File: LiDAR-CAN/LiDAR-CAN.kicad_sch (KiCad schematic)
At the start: 32 parts, among them J1 XT30(2+2), J2 XT30(2+2), J3 G7LX-A88S7-BP-G/Y, J4 XT30(2+2)

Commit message: Add CAN and MCU placement
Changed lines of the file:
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@@
 	)
 	(junction
-		(at 270.51 127)
+		(at 158.75 165.1)
 		(diameter 0)
 		(color 0 0 0 0)
 	)
 	(junction
-		(at 158.75 120.65)
+		(at 270.51 127)
 		(diameter 0)
 		(color 0 0 0 0)
 	)
 	(junction
-		(at 158.75 167.64)
+		(at 158.75 123.19)
 		(diameter 0)
 		(color 0 0 0 0)
 	)
 	(junction
-		(at 158.75 162.56)
+		(at 260.35 222.25)
 		(diameter 0)
 		(color 0 0 0 0)
 	)
 	(junction
-		(at 260.35 222.25)
+		(at 158.75 160.02)
 		(diameter 0)
 		(color 0 0 0 0)
 	)
 	(junction
-		(at 158.75 123.19)
+		(at 158.75 120.65)
 		(diameter 0)
 		(color 0 0 0 0)
@@
 	)
 	(junction
-		(at 158.75 160.02)
+		(at 158.75 162.56)
 		(diameter 0)
 		(color 0 0 0 0)
 	)
 	(junction
-		(at 266.7 209.55)
+		(at 158.75 128.27)
 		(diameter 0)
 		(color 0 0 0 0)
 	)
 	(junction
-		(at 158.75 128.27)
+		(at 266.7 209.55)
 		(diameter 0)
 		(color 0 0 0 0)
@@
 	)
 	(junction
-		(at 158.75 165.1)
+		(at 304.8 209.55)
 		(diameter 0)
 		(color 0 0 0 0)
 	)
 	(junction
-		(at 304.8 209.55)
+		(at 292.1 209.55)
 		(diameter 0)
 		(color 0 0 0 0)
 	)
 	(junction
-		(at 292.1 209.55)
+		(at 158.75 167.64)
 		(diameter 0)
 		(color 0 0 0 0)
@@
 	(wire
 		(pts
-			(xy 152.4 123.19) (xy 158.75 123.19)
-		)
-		(stroke
-			(width 0)
-			(type default)
-		)
-	)
-	(wire
-		(pts
 			(xy 152.4 54.61) (xy 152.4 57.15)
 		)
@@
 	(wire
 		(pts
-			(xy 152.4 128.27) (xy 158.75 128.27)
-		)
-		(stroke
-			(width 0)
-			(type default)
-		)
-	)
-	(wire
-		(pts
 			(xy 158.75 123.19) (xy 181.61 123.19)
 		)
@@
 	(wire
 		(pts
-			(xy 152.4 162.56) (xy 158.75 162.56)
+			(xy 152.4 120.65) (xy 158.75 120.65)
 		)
 		(stroke
@@
 	(wire
 		(pts
-			(xy 152.4 165.1) (xy 158.75 165.1)
+			(xy 189.23 208.28) (xy 189.23 165.1)
 		)
 		(stroke
@@
 	(wire
 		(pts
-			(xy 189.23 208.28) (xy 189.23 165.1)
+			(xy 152.4 125.73) (xy 158.75 125.73)
 		)
 		(stroke
@@
 	(wire
 		(pts
+			(xy 152.4 167.64) (xy 158.75 167.64)
+		)
+		(stroke
+			(width 0)
+			(type default)
+		)
+	)
+	(wire
+		(pts
 			(xy 210.82 76.2) (xy 210.82 81.28)
 		)
@@
 	(wire
 		(pts
-			(xy 304.8 209.55) (xy 304.8 212.09)
+			(xy 152.4 160.02) (xy 158.75 160.02)
 		)
 		(stroke
@@
 	(wire
 		(pts
-			(xy 266.7 209.55) (xy 266.7 212.09)
+			(xy 304.8 209.55) (xy 304.8 212.09)
 		)
 		(stroke
@@
 	(wire
 		(pts
-			(xy 158.75 160.02) (xy 152.4 160.02)
+			(xy 266.7 209.55) (xy 266.7 212.09)
 		)
 		(stroke
@@
 	(wire
 		(pts
-			(xy 152.4 167.64) (xy 158.75 167.64)
-		)
-		(stroke
-			(width 0)
-			(type default)
-		)
-	)
-	(wire
-		(pts
 			(xy 332.74 203.2) (xy 330.2 205.74)
 		)
@@
 	(wire
 		(pts
+			(xy 152.4 165.1) (xy 158.75 165.1)
+		)
+		(stroke
+			(width 0)
+			(type default)
+		)
+	)
+	(wire
+		(pts
 			(xy 260.35 222.25) (xy 266.7 222.25)
 		)
@@
 	(wire
 		(pts
-			(xy 270.51 127) (xy 279.4 127)
+			(xy 152.4 162.56) (xy 158.75 162.56)
 		)
 		(stroke
@@
 	(wire
 		(pts
-			(xy 158.75 120.65) (xy 179.07 120.65)
+			(xy 270.51 127) (xy 279.4 127)
 		)
 		(stroke
@@
 	(wire
 		(pts
-			(xy 241.3 93.98) (xy 285.75 93.98)
+			(xy 158.75 120.65) (xy 179.07 120.65)
 		)
 		(stroke
@@
 	(wire
 		(pts
-			(xy 266.7 127) (xy 266.7 129.54)
+			(xy 241.3 93.98) (xy 285.75 93.98)
 		)
 		(stroke
@@
 	(wire
 		(pts
-			(xy 179.07 120.65) (xy 179.07 88.9)
+			(xy 266.7 127) (xy 266.7 129.54)
 		)
 		(stroke
@@
 	(wire
 		(pts
-			(xy 317.5 205.74) (xy 330.2 205.74)
+			(xy 152.4 128.27) (xy 158.75 128.27)
 		)
 		(stroke
@@
 	(wire
 		(pts
-			(xy 241.3 104.14) (xy 285.75 104.14)
+			(xy 179.07 120.65) (xy 179.07 88.9)
 		)
 		(stroke
@@
 	(wire
 		(pts
-			(xy 254 212.09) (xy 254 203.2)
+			(xy 317.5 205.74) (xy 330.2 205.74)
 		)
 		(stroke
@@
 	(wire
 		(pts
-			(xy 262.89 111.76) (xy 262.89 118.11)
+			(xy 241.3 104.14) (xy 285.75 104.14)
 		)
 		(stroke
@@
 	(wire
 		(pts
-			(xy 215.9 203.2) (xy 194.31 203.2)
+			(xy 254 212.09) (xy 254 203.2)
 		)
 		(stroke
@@
 	(wire
 		(pts
-			(xy 152.4 125.73) (xy 158.75 125.73)
+			(xy 262.89 111.76) (xy 262.89 118.11)
 		)
 		(stroke
@@
 	(wire
 		(pts
-			(xy 285.75 116.84) (xy 279.4 116.84)
+			(xy 215.9 203.2) (xy 194.31 203.2)
 		)
 		(stroke
@@
 	(wire
 		(pts
-			(xy 215.9 226.06) (xy 171.45 226.06)
+			(xy 285.75 116.84) (xy 279.4 116.84)
 		)
 		(stroke
@@
 	(wire
 		(pts
-			(xy 152.4 120.65) (xy 158.75 120.65)
+			(xy 215.9 226.06) (xy 171.45 226.06)
 		)
 		(stroke
@@
 		)
 	)
+	(wire
+		(pts
+			(xy 152.4 123.19) (xy 158.75 123.19)
+		)
+		(stroke
+			(width 0)
+			(type default)
+		)
+	)
 	(symbol
 		(lib_id "Connector:TestPoint_Small")
@@
 		)
 		(pin "SPI1_MISO" input
-			(at 152.4 125.73 0)
+			(at 152.4 165.1 0)
 			(effects
 				(font
@@
 		)
 		(pin "SPI1_MOSI" output
-			(at 152.4 123.19 0)
+			(at 152.4 162.56 0)
 			(effects
 				(font
@@
 		)
 		(pin "SPI1_NSS" output
-			(at 152.4 128.27 0)
+			(at 152.4 167.64 0)
 			(effects
 				(font
@@
 		)
 		(pin "SPI1_SCK" output
-			(at 152.4 120.65 0)
+			(at 152.4 160.02 0)
 			(effects
 				(font
@@
 		)
 		(pin "SPI2_MISO" input
-			(at 152.4 162.56 0)
+			(at 152.4 125.73 0)
 			(effects
 				(font
@@
 		)
 		(pin "SPI2_MOSI" output
-			(at 152.4 165.1 0)
+			(at 152.4 123.19 0)
 			(effects
 				(font
@@
 		)
 		(pin "SPI2_NSS" output
-			(at 152.4 167.64 0)
+			(at 152.4 128.27 0)
 			(effects
 				(font
@@
 		)
 		(pin "SPI2_SCK" output
-			(at 152.4 160.02 0)
+			(at 152.4 120.65 0)
 			(effects
 				(font

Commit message: Update complete first placement
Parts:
- added H3: MountingHole, MountingHole:MountingHole_2.2mm_M2, symbol Mechanical:MountingHole
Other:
- moved on the sheet: FID1, FID2, H1, H2
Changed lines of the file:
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@@
 	(text_box "Mechanicals"
 		(exclude_from_sim no)
-		(at 50.8 215.9 0)
-		(size 88.9 25.4)
+		(at 38.1 215.9 0)
+		(size 101.6 25.4)
 		(margins 0.9525 0.9525 0.9525 0.9525)
 		(stroke
@@
 	)
 	(symbol
+		(lib_id "Mechanical:MountingHole")
+		(at 120.65 228.6 0)
+		(unit 1)
+		(exclude_from_sim yes)
+		(in_bom no)
+		(on_board yes)
+		(dnp no)
+		(fields_autoplaced yes)
+		(property "Reference" "H3"
+			(at 123.19 227.3299 0)
+			(effects
+				(font
+					(size 1.27 1.27)
+				)
+				(justify left)
+			)
+		)
+		(property "Value" "MountingHole"
+			(at 123.19 229.8699 0)
+			(effects
+				(font
+					(size 1.27 1.27)
+				)
+				(justify left)
+			)
+		)
+		(property "Footprint" "MountingHole:MountingHole_2.2mm_M2"
+			(at 120.65 228.6 0)
+			(effects
+				(font
+					(size 1.27 1.27)
+				)
+				(hide yes)
+			)
+		)
+		(property "Datasheet" "~"
+			(at 120.65 228.6 0)
+			(effects
+				(font
+					(size 1.27 1.27)
+				)
+				(hide yes)
+			)
+		)
+		(property "Description" "Mounting Hole without connection"
+			(at 120.65 228.6 0)
+			(effects
+				(font
+					(size 1.27 1.27)
+				)
+				(hide yes)
+			)
+		)
+		(instances
+			(project "LiDAR-CAN"
+				(path "/56db6f21-0e4a-4321-bd8a-db37f1842dd9"
+					(reference "H3")
+					(unit 1)
+				)
+			)
+		)
+	)
+	(symbol
 		(lib_id "Device:R_US")
 		(at 254 121.92 0)
@@
 	(symbol
 		(lib_id "Mechanical:Fiducial")
-		(at 63.5 228.6 0)
+		(at 50.8 228.6 0)
 		(unit 1)
 		(exclude_from_sim yes)
@@
 		(fields_autoplaced yes)
 		(property "Reference" "FID1"
-			(at 66.04 227.3299 0)
+			(at 53.34 227.3299 0)
 			(effects
 				(font
@@
 		)
 		(property "Value" "Fiducial"
-			(at 66.04 229.8699 0)
+			(at 53.34 229.8699 0)
 			(effects
 				(font
@@
 		)
 		(property "Footprint" "Fiducial:Fiducial_1.5mm_Mask3mm"
-			(at 63.5 228.6 0)
+			(at 50.8 228.6 0)
 			(effects
 				(font
@@
 		)
 		(property "Datasheet" "~"
-			(at 63.5 228.6 0)
+			(at 50.8 228.6 0)
 			(effects
 				(font
@@
 		)
 		(property "Description" "Fiducial Marker"
-			(at 63.5 228.6 0)
+			(at 50.8 228.6 0)
 			(effects
 				(font
@@
 	(symbol
 		(lib_id "Mechanical:Fiducial")
-		(at 76.2 228.6 0)
+		(at 63.5 228.6 0)
 		(unit 1)
 		(exclude_from_sim yes)
@@
 		(fields_autoplaced yes)
 		(property "Reference" "FID2"
-			(at 78.74 227.3299 0)
+			(at 66.04 227.3299 0)
 			(effects
 				(font
@@
 		)
 		(property "Value" "Fiducial"
-			(at 78.74 229.8699 0)
+			(at 66.04 229.8699 0)
 			(effects
 				(font
@@
 		)
 		(property "Footprint" "Fiducial:Fiducial_1.5mm_Mask3mm"
-			(at 76.2 228.6 0)
+			(at 63.5 228.6 0)
 			(effects
 				(font
@@
 		)
 		(property "Datasheet" "~"
-			(at 76.2 228.6 0)
+			(at 63.5 228.6 0)
 			(effects
 				(font
@@
 		)
 		(property "Description" "Fiducial Marker"
-			(at 76.2 228.6 0)
+			(at 63.5 228.6 0)
 			(effects
 				(font
@@
 	(symbol
 		(lib_id "Mechanical:MountingHole")
-		(at 95.25 228.6 0)
+		(at 82.55 228.6 0)
 		(unit 1)
 		(exclude_from_sim yes)
@@
 		(fields_autoplaced yes)
 		(property "Reference" "H1"
-			(at 97.79 227.3299 0)
+			(at 85.09 227.3299 0)
 			(effects
 				(font
@@
 		)
 		(property "Value" "MountingHole"
-			(at 97.79 229.8699 0)
+			(at 85.09 229.8699 0)
 			(effects
 				(font
@@
 		)
 		(property "Footprint" "MountingHole:MountingHole_2.2mm_M2"
-			(at 95.25 228.6 0)
+			(at 82.55 228.6 0)
 			(effects
 				(font
@@
 		)
 		(property "Datasheet" "~"
-			(at 95.25 228.6 0)
+			(at 82.55 228.6 0)
 			(effects
 				(font
@@
 		)
 		(property "Description" "Mounting Hole without connection"
-			(at 95.25 228.6 0)
+			(at 82.55 228.6 0)
 			(effects
 				(font
@@
 	(symbol
 		(lib_id "Mechanical:MountingHole")
-		(at 114.3 228.6 0)
+		(at 101.6 228.6 0)
 		(unit 1)
 		(exclude_from_sim yes)
@@
 		(fields_autoplaced yes)
 		(property "Reference" "H2"
-			(at 116.84 227.3299 0)
+			(at 104.14 227.3299 0)
 			(effects
 				(font
@@
 		)
 		(property "Value" "MountingHole"
-			(at 116.84 229.8699 0)
+			(at 104.14 229.8699 0)
 			(effects
 				(font
@@
 		)
 		(property "Footprint" "MountingHole:MountingHole_2.2mm_M2"
-			(at 114.3 228.6 0)
+			(at 101.6 228.6 0)
 			(effects
 				(font
@@
 		)
 		(property "Datasheet" "~"
-			(at 114.3 228.6 0)
+			(at 101.6 228.6 0)
 			(effects
 				(font
@@
 		)
 		(property "Description" "Mounting Hole without connection"
-			(at 114.3 228.6 0)
+			(at 101.6 228.6 0)
 			(effects
 				(font

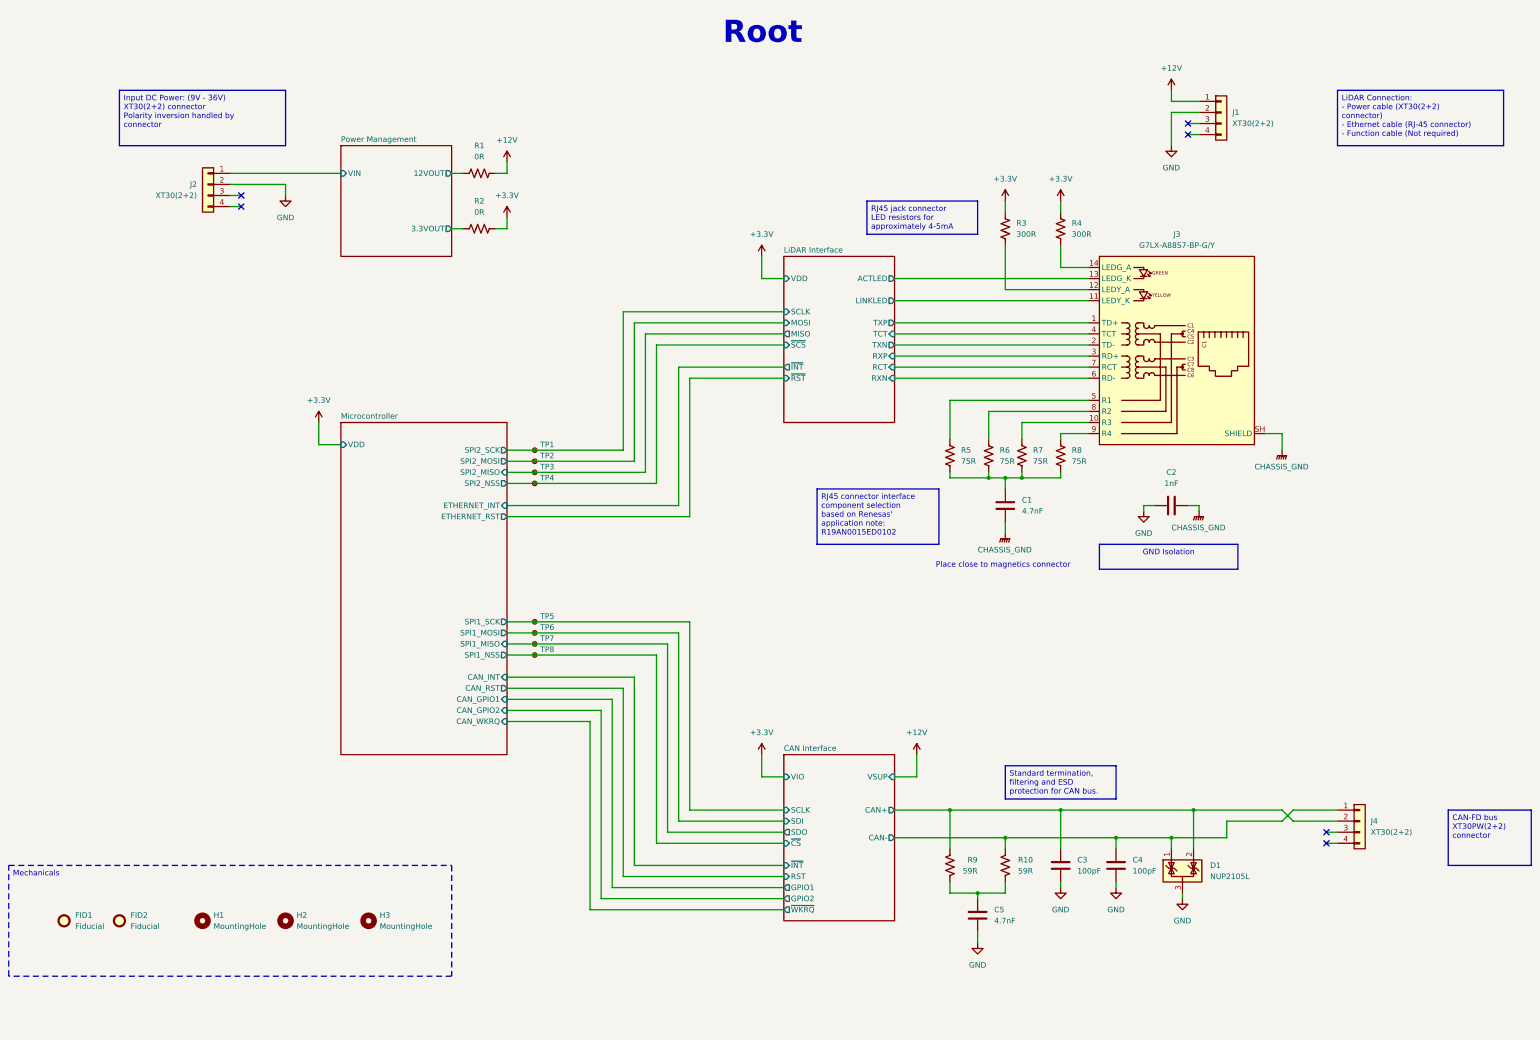
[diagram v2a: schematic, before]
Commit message: Feature schematic revision 2
Main changes related to connection wires for easy layout and minor components adjustments from Rev 1
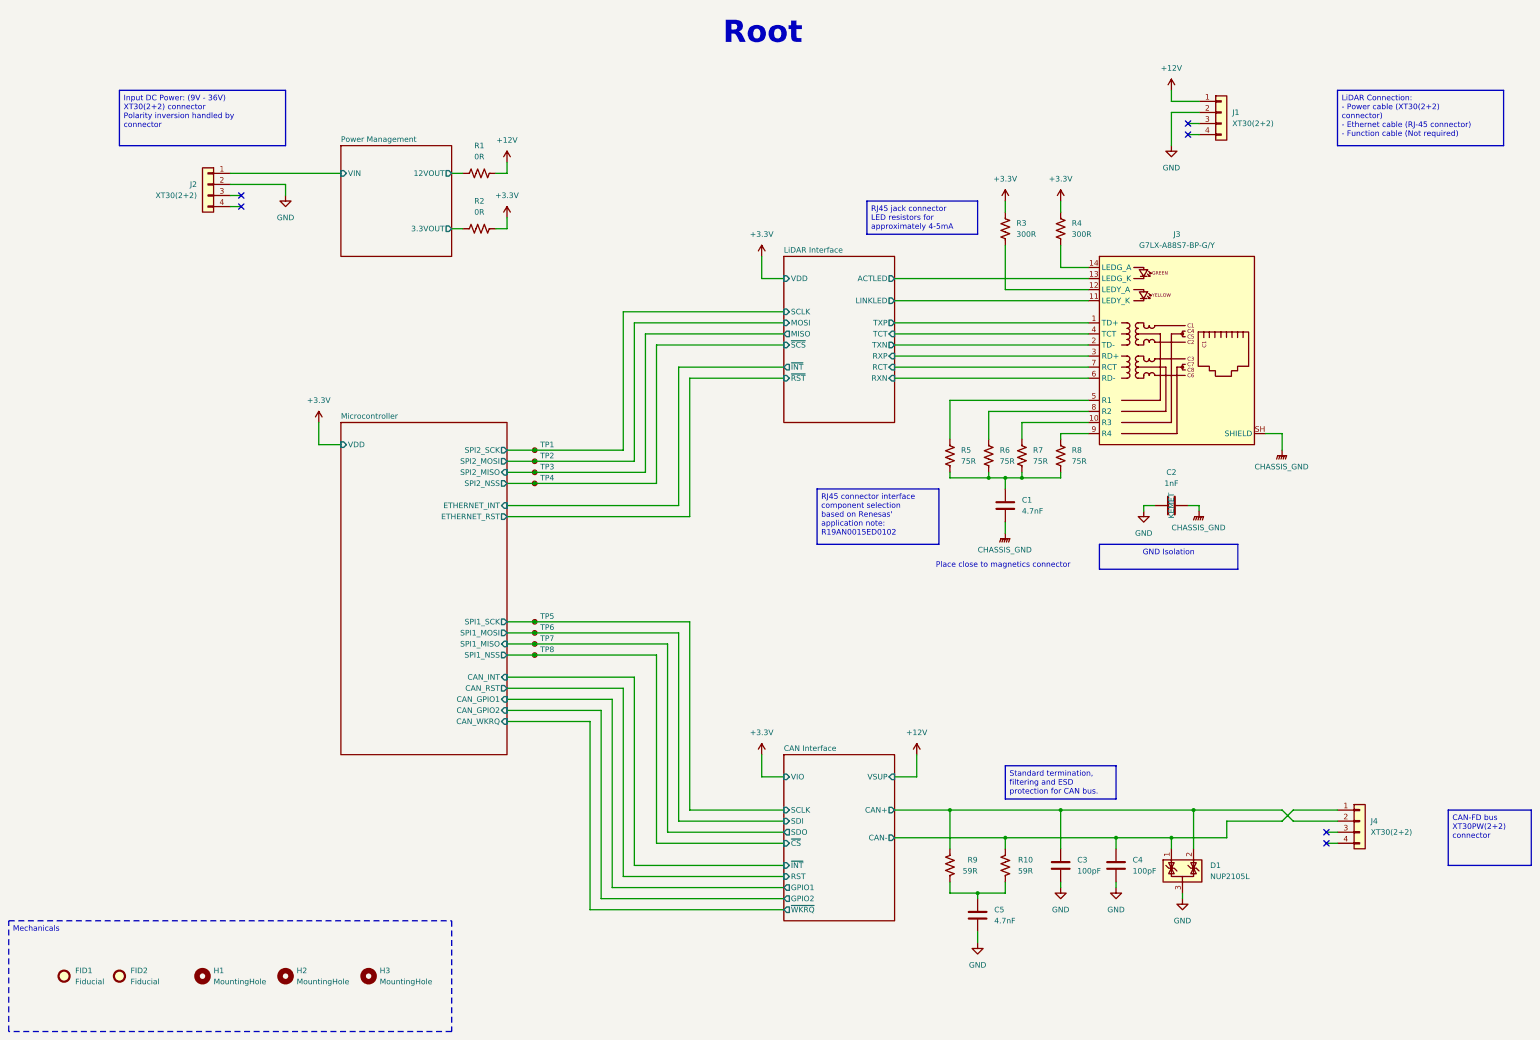
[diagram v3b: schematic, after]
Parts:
- C2: Manufacturer (none) -> KEMET
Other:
- moved on the sheet: FID1, FID2, H1, H2, H3
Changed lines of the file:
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@@
 	(title_block
 		(title "LiDAR-CAN Interface")
-		(date "2025-08-03")
-		(rev "1")
+		(date "2025-08-05")
+		(rev "2")
 		(company "Robot.com")
 	)
@@
 	(text_box "Mechanicals"
 		(exclude_from_sim no)
-		(at 38.1 215.9 0)
+		(at 38.1 228.6 0)
 		(size 101.6 25.4)
 		(margins 0.9525 0.9525 0.9525 0.9525)
@@
 	(symbol
 		(lib_id "Mechanical:MountingHole")
-		(at 120.65 228.6 0)
+		(at 120.65 241.3 0)
 		(unit 1)
 		(exclude_from_sim yes)
@@
 		(fields_autoplaced yes)
 		(property "Reference" "H3"
-			(at 123.19 227.3299 0)
+			(at 123.19 240.0299 0)
 			(effects
 				(font
@@
 		)
 		(property "Value" "MountingHole"
-			(at 123.19 229.8699 0)
+			(at 123.19 242.5699 0)
 			(effects
 				(font
@@
 		)
 		(property "Footprint" "MountingHole:MountingHole_2.2mm_M2"
-			(at 120.65 228.6 0)
+			(at 120.65 241.3 0)
 			(effects
 				(font
@@
 		)
 		(property "Datasheet" "~"
-			(at 120.65 228.6 0)
+			(at 120.65 241.3 0)
 			(effects
 				(font
@@
 		)
 		(property "Description" "Mounting Hole without connection"
-			(at 120.65 228.6 0)
+			(at 120.65 241.3 0)
 			(effects
 				(font
@@
 	(symbol
 		(lib_id "Mechanical:Fiducial")
-		(at 50.8 228.6 0)
+		(at 50.8 241.3 0)
 		(unit 1)
 		(exclude_from_sim yes)
@@
 		(fields_autoplaced yes)
 		(property "Reference" "FID1"
-			(at 53.34 227.3299 0)
+			(at 53.34 240.0299 0)
 			(effects
 				(font
@@
 		)
 		(property "Value" "Fiducial"
-			(at 53.34 229.8699 0)
+			(at 53.34 242.5699 0)
 			(effects
 				(font
@@
 		)
 		(property "Footprint" "Fiducial:Fiducial_1.5mm_Mask3mm"
-			(at 50.8 228.6 0)
+			(at 50.8 241.3 0)
 			(effects
 				(font
@@
 		)
 		(property "Datasheet" "~"
-			(at 50.8 228.6 0)
+			(at 50.8 241.3 0)
 			(effects
 				(font
@@
 		)
 		(property "Description" "Fiducial Marker"
-			(at 50.8 228.6 0)
+			(at 50.8 241.3 0)
 			(effects
 				(font
@@
 	(symbol
 		(lib_id "Mechanical:Fiducial")
-		(at 63.5 228.6 0)
+		(at 63.5 241.3 0)
 		(unit 1)
 		(exclude_from_sim yes)
@@
 		(fields_autoplaced yes)
 		(property "Reference" "FID2"
-			(at 66.04 227.3299 0)
+			(at 66.04 240.0299 0)
 			(effects
 				(font
@@
 		)
 		(property "Value" "Fiducial"
-			(at 66.04 229.8699 0)
+			(at 66.04 242.5699 0)
 			(effects
 				(font
@@
 		)
 		(property "Footprint" "Fiducial:Fiducial_1.5mm_Mask3mm"
-			(at 63.5 228.6 0)
+			(at 63.5 241.3 0)
 			(effects
 				(font
@@
 		)
 		(property "Datasheet" "~"
-			(at 63.5 228.6 0)
+			(at 63.5 241.3 0)
 			(effects
 				(font
@@
 		)
 		(property "Description" "Fiducial Marker"
-			(at 63.5 228.6 0)
+			(at 63.5 241.3 0)
 			(effects
 				(font
@@
 	(symbol
 		(lib_id "Mechanical:MountingHole")
-		(at 82.55 228.6 0)
+		(at 82.55 241.3 0)
 		(unit 1)
 		(exclude_from_sim yes)
@@
 		(fields_autoplaced yes)
 		(property "Reference" "H1"
-			(at 85.09 227.3299 0)
+			(at 85.09 240.0299 0)
 			(effects
 				(font
@@
 		)
 		(property "Value" "MountingHole"
-			(at 85.09 229.8699 0)
+			(at 85.09 242.5699 0)
 			(effects
 				(font
@@
 		)
 		(property "Footprint" "MountingHole:MountingHole_2.2mm_M2"
-			(at 82.55 228.6 0)
+			(at 82.55 241.3 0)
 			(effects
 				(font
@@
 		)
 		(property "Datasheet" "~"
-			(at 82.55 228.6 0)
+			(at 82.55 241.3 0)
 			(effects
 				(font
@@
 		)
 		(property "Description" "Mounting Hole without connection"
-			(at 82.55 228.6 0)
+			(at 82.55 241.3 0)
 			(effects
 				(font
@@
 			)
 		)
-		(property "Datasheet" "https://content.kemet.com/datasheets/KEM_C1076_X7R_HV_AUTO_SMD.pdf"
+		(property "Datasheet" "https://search.kemet.com/download/datasheet/C1808C102MGRACAUTO"
 			(at 304.8 133.35 0)
 			(effects
@@
 			)
 		)
-		(property "Description" "1000 pF ±20% 2000V (2kV) Ceramic Capacitor X7R 1808 (4520 Metric)"
+		(property "Description" "CAP CER 1808 1NF 2000V X7R 20%"
 			(at 304.8 133.35 0)
 			(effects
@@
 			)
 		)
+		(property "Manufacturer" "KEMET"
+			(at 304.8 133.35 0)
+			(effects
+				(font
+					(size 1.27 1.27)
+				)
+			)
+		)
 		(pin "1"
 		)
@@
 	(symbol
 		(lib_id "Mechanical:MountingHole")
-		(at 101.6 228.6 0)
+		(at 101.6 241.3 0)
 		(unit 1)
 		(exclude_from_sim yes)
@@
 		(fields_autoplaced yes)
 		(property "Reference" "H2"
-			(at 104.14 227.3299 0)
+			(at 104.14 240.0299 0)
 			(effects
 				(font
@@
 		)
 		(property "Value" "MountingHole"
-			(at 104.14 229.8699 0)
+			(at 104.14 242.5699 0)
 			(effects
 				(font
@@
 		)
 		(property "Footprint" "MountingHole:MountingHole_2.2mm_M2"
-			(at 101.6 228.6 0)
+			(at 101.6 241.3 0)
 			(effects
 				(font
@@
 		)
 		(property "Datasheet" "~"
-			(at 101.6 228.6 0)
+			(at 101.6 241.3 0)
 			(effects
 				(font
@@
 		)
 		(property "Description" "Mounting Hole without connection"
-			(at 101.6 228.6 0)
+			(at 101.6 241.3 0)
 			(effects
 				(font
